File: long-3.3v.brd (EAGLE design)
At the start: 50 x 50 mm, 44 parts, among them J1 CON_HEADER_1X06-SMD-RIGHT-ANG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, Q1 BSS84, U2 MCP73831, U3 MCP9808T-E/MC, U4 ADXL375BCCZ, X1 Micro USB, X2 CRYSTAL, X3 CRYSTALS-NOGND-IQXC-25

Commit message: Changed layout, routed board
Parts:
- removed JP14, JP15, JP16, JP17: M02PTH, SparkFun-Connectors:1X02
- removed U$2: UBLOX_MAX, Ava:UBLOX_MAX
- removed U4: ADXL375BCCZ, adxl375bccz:LGA_CC-14-1
- added C15: 100nF, rcl:C0402
- added R6, R8: 3k3, SparkFun:0402-RES
- JP1, JP2: device SparkFun:1X05 -> SparkFun:1X03
- JP3, JP4: device SparkFun:1X07 -> SparkFun:1X05
- moved R2 44.2 mm to (5.60, 48.2), flipped to the top, turned to 270 degrees
- moved R5 42.1 mm to (9.80, 48.2), flipped to the top, turned to 270 degrees
- moved C14 41.8 mm to (9.28, 44.6), turned to 90 degrees
- moved R7 39.8 mm to (15.0, 48.2), flipped to the top, turned to 270 degrees
- moved U3 38.5 mm to (6.50, 44.2), turned to 0 degrees
- moved Q1 35.4 mm to (12.5, 48.2), flipped to the top, turned to 90 degrees
- moved JP2 30.4 mm to (18.7, 43.5), turned to 270 degrees
- moved JP3 23.2 mm to (1.30, 18.1), turned to 270 degrees
- moved JP4 19.9 mm to (18.7, 18.1), turned to 270 degrees
- moved C8 17.6 mm to (11.7, 46.0), flipped to the top
- moved C10 17.2 mm to (3.08, 13.4), flipped to the top, turned to 270 degrees
- moved IC1 14.2 mm to (4.70, 10.3), flipped to the top
- moved C13 12.5 mm to (8.75, 8.60), turned to 90 degrees
- moved C12 11.4 mm to (9.80, 10.6)
- moved C5 11.4 mm to (15.9, 18.2), turned to 0 degrees
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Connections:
- removed net UART_RX: JP4.6
- removed net UART_TX: JP4.7
- net EXT_CS: now also JP4.3; no longer JP1.5, JP2.5
- net EXT_MISO: now also JP4.4; no longer JP1.3, JP2.3
- net EXT_MOSI: now also JP4.2; no longer JP1.2, JP2.2
- net EXT_RX: now also JP2.2; no longer JP3.6
- net EXT_SCK: now also JP4.5; no longer JP1.4, JP2.4
- net EXT_TX: now also JP2.3; no longer JP3.7
- net GND: now also C15.2, JP1.3; no longer JP15.2, JP17.2, U$2.10_GND, U$2.12_GND, U$2.1_GND, U4.2, U4.4, U4.5
- net GPIO1: no longer JP4.1
- net GPIO2: no longer JP4.2
- net GPIO3: no longer JP4.3
- net GPIO4: now also JP3.4; no longer JP1.1, JP2.1
- net GPS_RX: now also JP4.1; no longer JP14.2, JP16.2, U$2.3_RXD1
- net GPS_TX: now also JP3.5; no longer JP14.1, JP16.1, U$2.2_TXD1
- net I2C_SCL: now also JP1.1; no longer JP3.4, JP4.4, U4.14
- net I2C_SDA: now also JP2.1; no longer JP3.5, JP4.5, U4.13
- net LOCAL_SCL: now also R8.2
- net LOCAL_SDA: now also R6.2
- net VCC: now also C15.1, R6.1, R8.1; no longer U$2.14_VCC_RF, U$2.6_V_BCKP, U$2.7_VCC_IO, U$2.8_VCC, U$2.9_V_RESET, U4.1, U4.6
- net VCC_SW: now also JP1.2; no longer JP15.1, JP17.1
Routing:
- net LOCAL_SDA: track 14.8 -> 54.5 mm, vias 2 -> 4
- net EXT_CS: track 55.8 -> 20.9 mm
- net LOCAL_SCL: track 27.4 -> 58.5 mm, vias 0 -> 4
- net EXT_SW: track 10.7 -> 39.4 mm, vias 1 -> 2
- net EXT_SCK: track 46.7 -> 18.4 mm, vias 2 -> 1
- net EXT_MISO: track 46.0 -> 18.7 mm, vias 2 -> 1
- net EXT_MOSI: track 45.6 -> 21.7 mm, vias 2 -> 1
- net FLASH_MISO: track 45.9 -> 23.3 mm
- net FLASH_CS: track 41.9 -> 19.6 mm
- net GND: track 148.2 -> 167.8 mm, vias 14 -> 9
- net VCC: track 137.5 -> 118.1 mm
- net GPIO4: track 35.2 -> 18.3 mm, vias 2 -> 1
- net GPIO3: track 32.9 -> 17.8 mm, vias 2 -> 1
- net EXT_TX: track 39.4 -> 24.9 mm
- net EXT_RX: track 39.6 -> 27.6 mm, vias 2 -> 1
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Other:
- board size 50 x 50 mm -> 20 x 50 mm

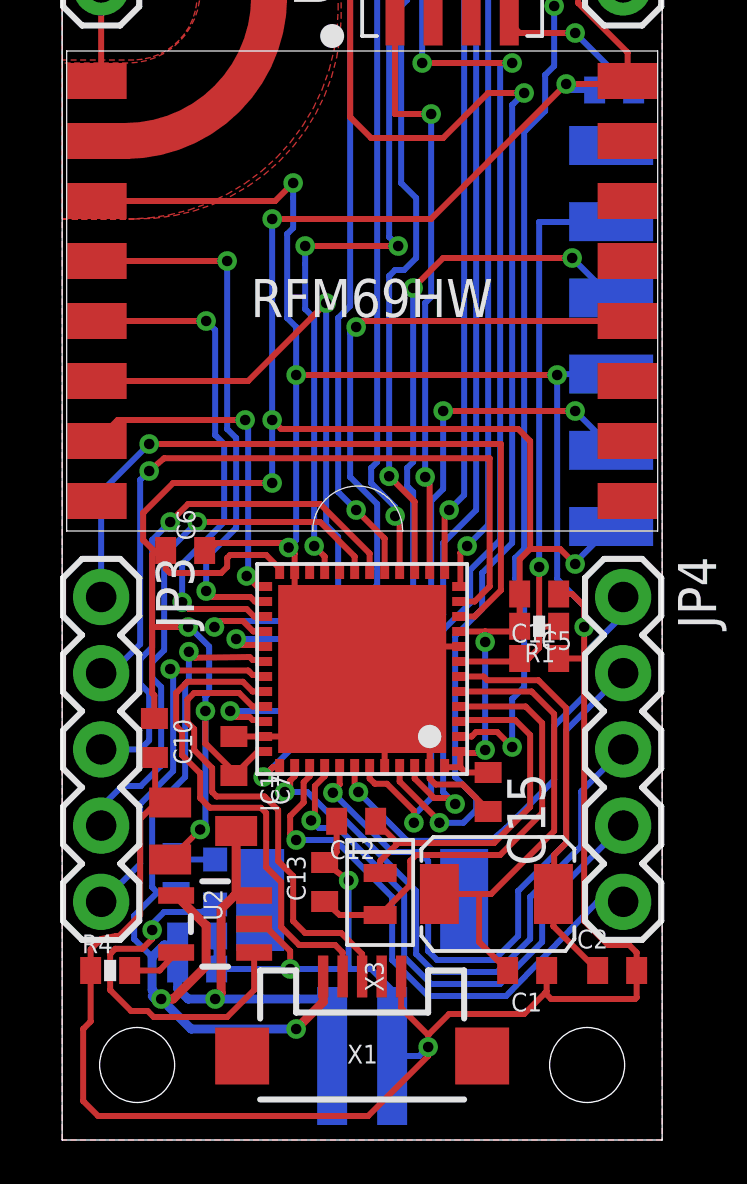
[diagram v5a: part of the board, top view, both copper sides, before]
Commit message: New layout routed
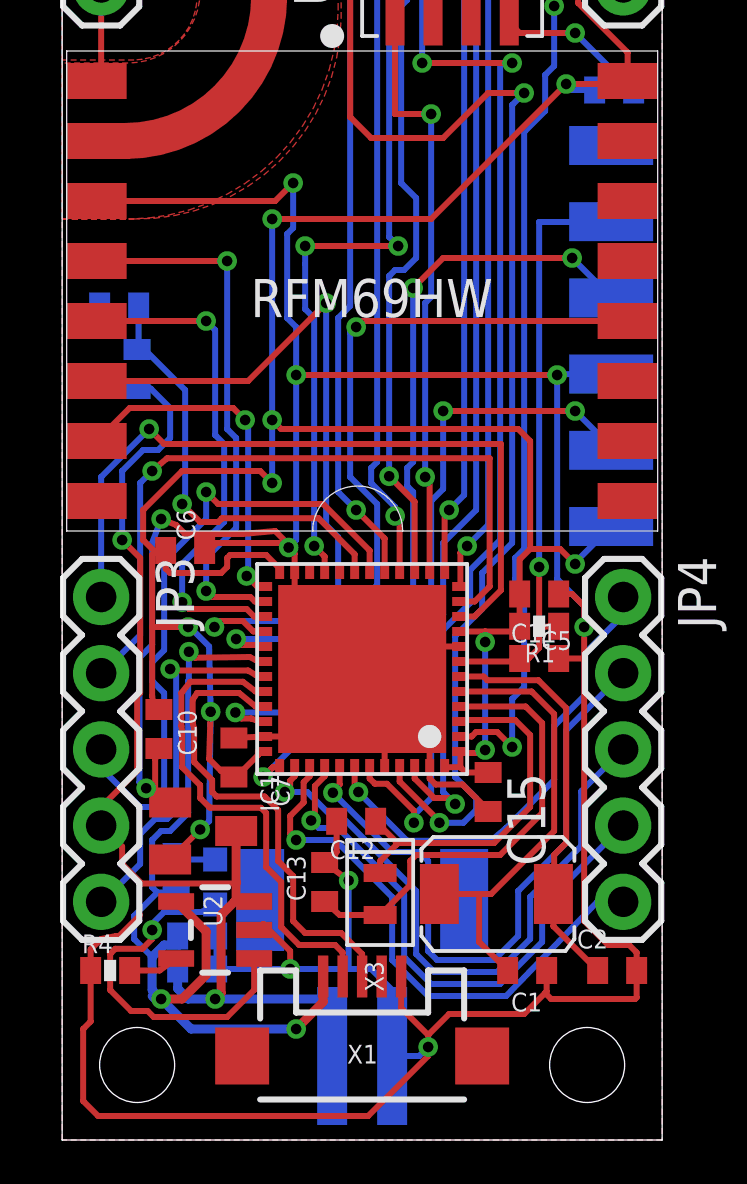
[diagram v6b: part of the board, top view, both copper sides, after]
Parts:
- added R10, R9: 10k, SparkFun:0402-RES
- moved C10 0.34 mm to (3.23, 13.7)
- moved U2 0.20 mm to (5.10, 7.00)
- moved C7 0.05 mm to (5.72, 12.8)
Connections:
- removed net GPIO4: JP3.4, U$1.P$19
- new net V_MEAS: R10.1, R9.2, U$1.P$19
- net GND: now also R10.2
- net VBAT: now also JP3.4, R9.1
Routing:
- net VBAT: track 14.9 -> 37.1 mm, vias 1 -> 2
- net GPIO4: track 18.3 -> 0.00 mm, vias 1 -> 0
- net V_MEAS: track 0.00 -> 14.5 mm, vias 0 -> 1
- net GND: track 167.8 -> 178.1 mm, vias 9 -> 11
- net GPIO3: track 17.8 -> 21.7 mm
- net VCC: track 118.1 -> 119.1 mm
- net GPIO1: track 24.1 -> 24.8 mm

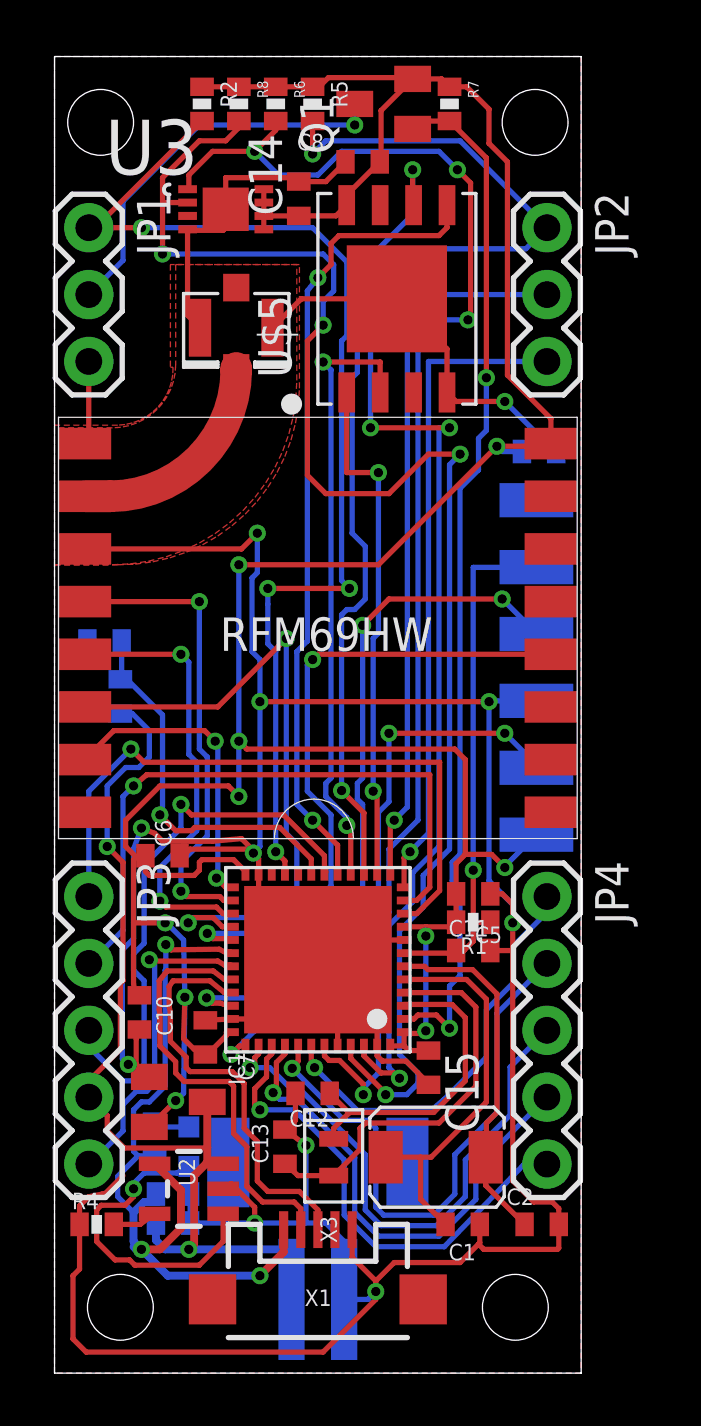
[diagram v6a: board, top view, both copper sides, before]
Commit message: done silk and mitred some bends
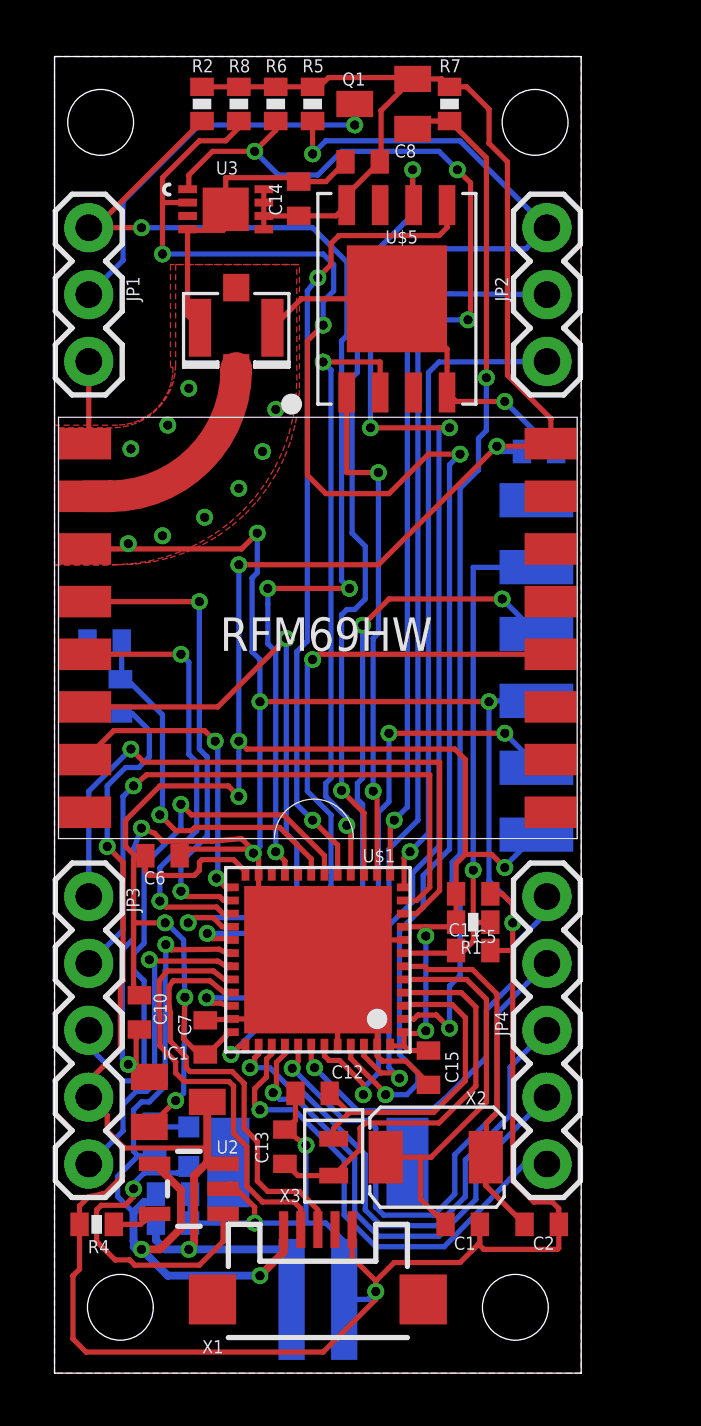
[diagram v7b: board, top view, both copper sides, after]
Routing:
- net GND: vias 11 -> 20
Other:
- board text added: "CS"
- board text added: "D11"
- board text added: "GPIO1"
- board text added: "GPIO2"
- board text added: "GPIO3"
- board text added: "MISO"
- board text added: "MOSI"
- board text added: "RX"
- board text added: "SCK"
- board text added: "SCL"
- board text added: "SDA"
- board text added: "TX"
- board text added: "U$1"
- board text added: "VBAT"
- board text added: "VCC"
- board text added: "X2"
- board text removed: "3.3V"
- board text removed: "RX2"
- board text removed: "TX2"

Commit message: updated RF
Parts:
- added C16, C17: (no value), rcl:C0402
- moved U$4 1.00 mm to (6.90, 40.7)
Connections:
- new net N$5: C16.1, C17.2, U$3.ANT
- net GND: now also C17.1
- net N$4: now also C16.2; no longer U$3.ANT
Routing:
- net N$5: track 0.00 -> 8.00 mm
- net N$4: track 7.81 -> 0.82 mm
- net GND: track 178.1 -> 177.7 mm, vias 20 -> 23
